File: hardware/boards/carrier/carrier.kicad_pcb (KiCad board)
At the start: 4 copper layers, 106 x 34.3 mm, 56 parts, among them J1 XT30PW(2+2), Q1 IPB020N10N5LF, Q2 2N7002, Q3 2N7002, SW1 SKSCLCE010, U1 STM32G031G6U6, U2 LM5163DDAR, U3 LMX5069MS, U4 INA237AIDGSR

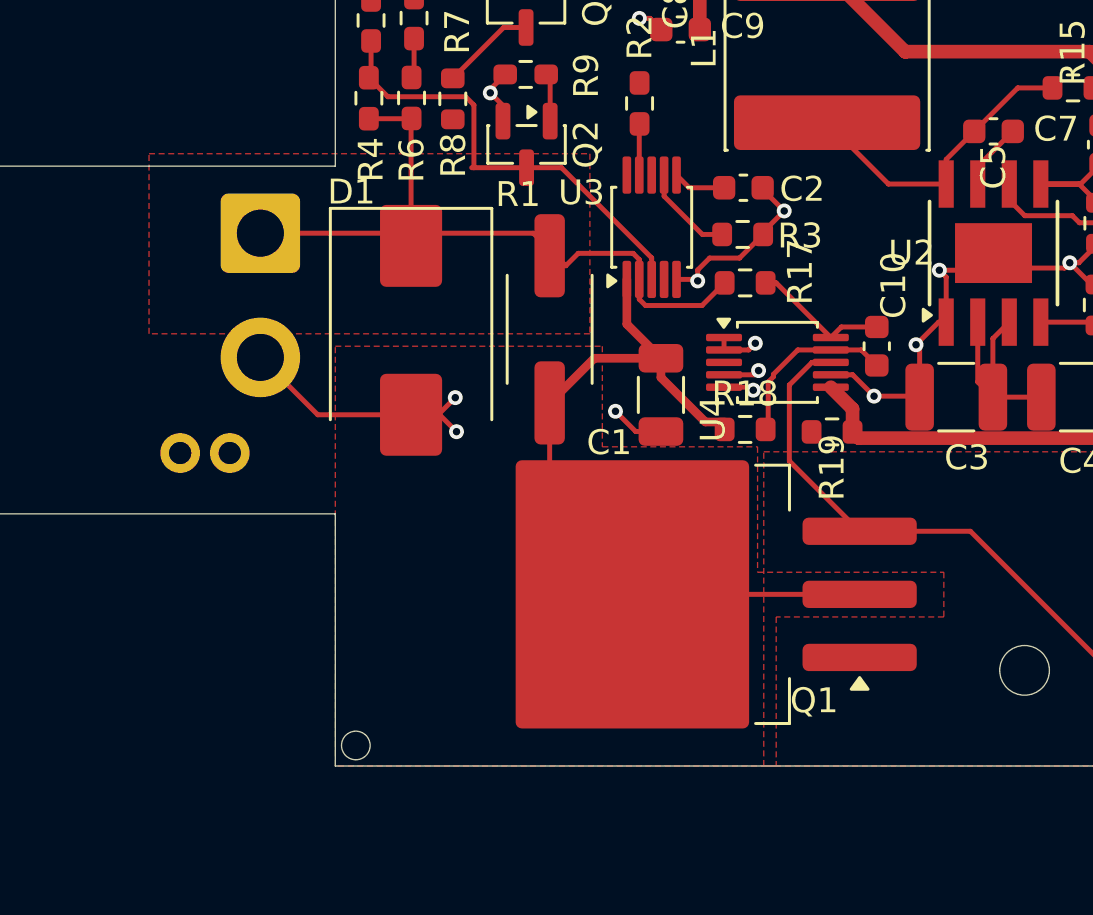
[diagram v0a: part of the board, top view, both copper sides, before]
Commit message: hardware: add HS_SENSE thermal plane and stitching vias
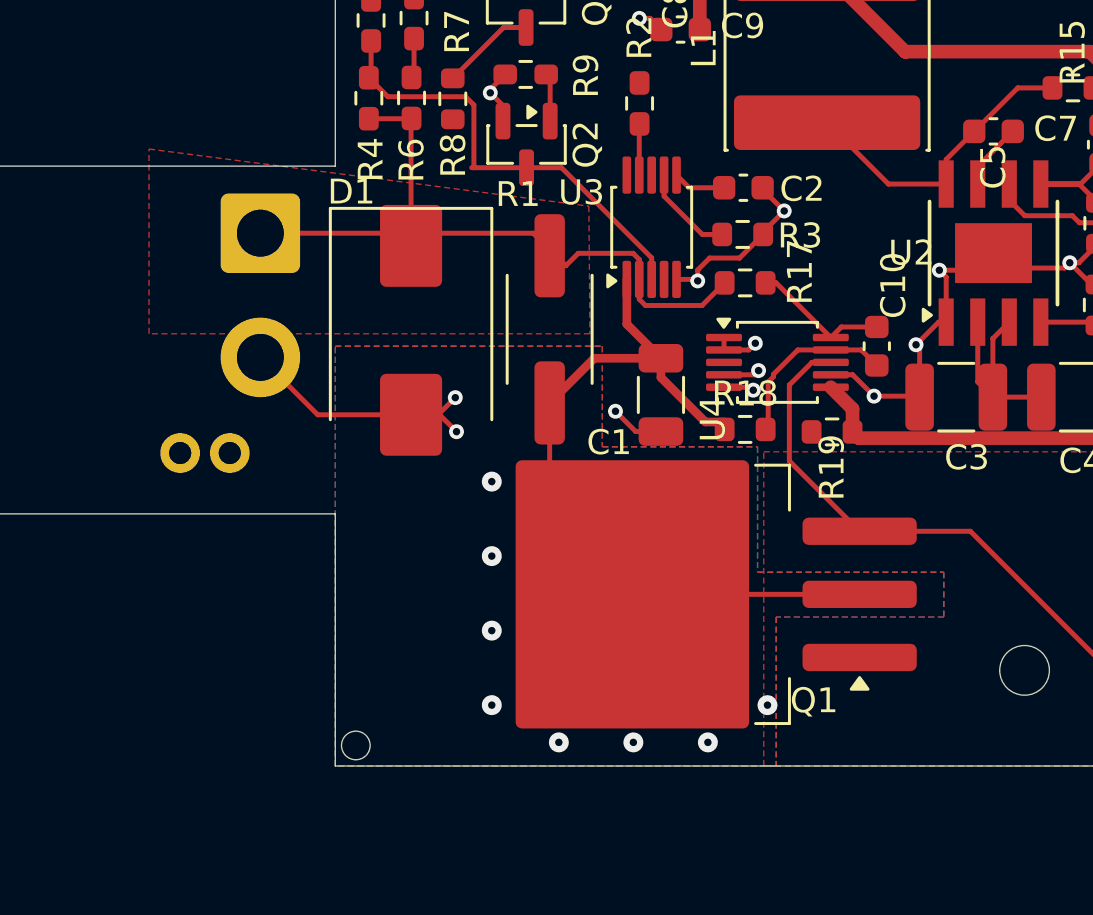
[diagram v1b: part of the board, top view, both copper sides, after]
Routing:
- net /Protected Power and Controls/HS_SENSE: vias 0 -> 8
- added copper zone on B.Cu, net /Protected Power and Controls/HS_SENSE
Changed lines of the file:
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@@
+		(net "/Protected Power and Controls/HS_SENSE")
+	)
+	(via
+		(at 121.8 128.2)
+		(size 0.8)
+		(drill 0.3)
+		(layers "F.Cu" "B.Cu")
+		(free yes)
+		(net "/Protected Power and Controls/HS_SENSE")
+	)
+	(via
+		(at 121.8 119.2)
+		(size 0.8)
+		(drill 0.3)
+		(layers "F.Cu" "B.Cu")
+		(free yes)
+		(net "/Protected Power and Controls/HS_SENSE")
+	)
+	(via
+		(at 121.8 125.2)
+		(size 0.8)
+		(drill 0.3)
+		(layers "F.Cu" "B.Cu")
+		(free yes)
+		(net "/Protected Power and Controls/HS_SENSE")
+	)
+	(via
+		(at 132.9 128.2)
+		(size 0.8)
+		(drill 0.3)
+		(layers "F.Cu" "B.Cu")
+		(free yes)
+		(net "/Protected Power and Controls/HS_SENSE")
+	)
+	(via
+		(at 130.5 129.7)
+		(size 0.8)
+		(drill 0.3)
+		(layers "F.Cu" "B.Cu")
+		(free yes)
+		(net "/Protected Power and Controls/HS_SENSE")
+	)
+	(via
+		(at 121.8 122.2)
+		(size 0.8)
+		(drill 0.3)
+		(layers "F.Cu" "B.Cu")
+		(free yes)
+		(net "/Protected Power and Controls/HS_SENSE")
+	)
+	(via
+		(at 124.5 129.7)
+		(size 0.8)
+		(drill 0.3)
+		(layers "F.Cu" "B.Cu")
+		(free yes)
+		(net "/Protected Power and Controls/HS_SENSE")
+	)
+	(via
+		(at 127.5 129.7)
+		(size 0.8)
+		(drill 0.3)
+		(layers "F.Cu" "B.Cu")
+		(free yes)
 		(net "/Protected Power and Controls/HS_SENSE")
 	)
@@
 		(layer "F.Cu")
 		(net "/STM32 Housekeeping and Status/NRST")
+	)
+	(zone
+		(net "/Protected Power and Controls/HS_SENSE")
+		(layer "F.Cu")
+		(name "HS_SENSE")
+		(hatch edge 0.5)
+		(priority 1)
+		(connect_pads
+			(clearance 0.5)
+		)
+		(min_thickness 0.25)
+		(fill yes
+			(thermal_gap 0.5)
+			(thermal_bridge_width 0.5)
+			(island_removal_mode 0)
+		)
+		(polygon
+			(pts
+				(xy 115.5 113.75) (xy 126.25 113.75) (xy 126.25 117.8) (xy 132.5 117.8) (xy 132.5 122.85) (xy 140 122.85)
+				(xy 140 124.65) (xy 133.25 124.65) (xy 133.25 130.65) (xy 115.5 130.65)
+			)
+		)
+	)
+	(zone
+		(net "VCC")
+		(layer "F.Cu")
+		(name "VCC")
+		(hatch edge 0.5)
+		(priority 2)
+		(connect_pads
+			(clearance 0.5)
+		)
+		(min_thickness 0.25)
+		(fill yes
+			(thermal_gap 0.5)
+			(thermal_bridge_width 0.5)
+			(island_removal_mode 0)
+		)
+		(polygon
+			(pts
+				(xy 108 105.810649) (xy 125.708468 108.11045) (xy 125.75 113.25) (xy 108 113.25)
+			)
+		)
+	)
+	(zone
+		(net "/Protected Power and Controls/PD_VIN_SW")
+		(layer "F.Cu")
+		(name "PD_VIN_SW")
+		(hatch edge 0.5)
+		(connect_pads
+			(clearance 0.5)
+		)
+		(min_thickness 0.25)
+		(fill yes
+			(thermal_gap 0.5)
+			(thermal_bridge_width 0.5)
+			(island_removal_mode 0)
+		)
+		(polygon
+			(pts
+				(xy 132.75 118) (xy 155.1 118) (xy 155.1 130.65) (xy 132.75 130.65)
+			)
+		)
+	)
+	(zone
+		(net "VCC")
+		(layer "F.Cu")
+		(hatch none 0.1)
+		(priority 30001)
+		(attr
+			(teardrop
+				(type padvia)
+			)
+		)
+		(connect_pads yes
+			(clearance 0)
+		)
+		(min_thickness 0.0254)
+		(fill yes
+			(island_removal_mode 1)
+		)
+		(polygon
+			(pts
+				(xy 115.0825 109.3) (xy 115.0825 109.1) (xy 114.0825 108.2) (xy 112.4815 109.2) (xy 114.0825 110.2)
+			)
+		)
 	)
 	(zone
@@
 	(zone
 		(net "/Protected Power and Controls/HS_SENSE")
-		(layer "F.Cu")
-		(name "HS_SENSE")
+		(layer "B.Cu")
+		(name "HS_SENSE_BOTTOM")
 		(hatch edge 0.5)
 		(priority 1)
@@
 		)
 		(min_thickness 0.25)
-		(fill
+		(fill yes
 			(thermal_gap 0.5)
 			(thermal_bridge_width 0.5)
@@
 		(polygon
 			(pts
-				(xy 115.5 113.75) (xy 126.25 113.75) (xy 126.25 117.8) (xy 132.5 117.8) (xy 132.5 122.85)
-				(xy 140 122.85) (xy 140 124.65) (xy 133.25 124.65) (xy 133.25 130.65) (xy 115.5 130.65)
+				(xy 115.5 113.75) (xy 126.25 113.75) (xy 126.25 117.8) (xy 132.5 117.8) (xy 132.5 122.85) (xy 140 122.85)
+				(xy 140 124.65) (xy 133.25 124.65) (xy 133.25 130.65) (xy 115.5 130.65)
 			)
 		)
-	)
-	(zone
-		(net "VCC")
-		(layer "F.Cu")
-		(name "VCC")
-		(hatch edge 0.5)
-		(priority 2)
-		(connect_pads
-			(clearance 0.5)
-		)
-		(min_thickness 0.25)
-		(fill
-			(thermal_gap 0.5)
-			(thermal_bridge_width 0.5)
-			(island_removal_mode 0)
-		)
-		(polygon
-			(pts
-				(xy 108 106) (xy 125.75 106) (xy 125.75 113.25) (xy 108 113.25)
-			)
-		)
-	)
-	(zone
-		(net "/Protected Power and Controls/PD_VIN_SW")
-		(layer "F.Cu")
-		(name "PD_VIN_SW")
-		(hatch edge 0.5)
-		(connect_pads
-			(clearance 0.5)
-		)
-		(min_thickness 0.25)
-		(fill
-			(thermal_gap 0.5)
-			(thermal_bridge_width 0.5)
-			(island_removal_mode 0)
-		)
-		(polygon
-			(pts
-				(xy 132.75 118) (xy 155.1 118) (xy 155.1 130.65) (xy 132.75 130.65)
-			)
-		)
-	)
-	(zone
-		(net "VCC")
-		(layer "F.Cu")
-		(hatch none 0.1)
-		(priority 30000)
-		(attr
-			(teardrop
-				(type padvia)
-			)
-		)
-		(connect_pads yes
-			(clearance 0)
-		)
-		(min_thickness 0.0254)
-		(fill yes
-			(island_removal_mode 1)
-		)
-		(polygon
-			(pts
-				(xy 115.0825 109.3) (xy 115.0825 109.1) (xy 114.0825 108.2) (xy 112.4815 109.2) (xy 114.0825 110.2)
-			)
-		)

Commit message: Checkpoint:
Routing is still ... in progress
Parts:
- moved J2 0.13 mm to (190.7, 98.2)
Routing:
- net /PD_ENABLE: track 65.3 -> 1.90 mm
- net +3V3: track 94.7 -> 157.3 mm
- net /STM32 Housekeeping and Status/SWCLK: track 0.00 -> 4.68 mm
- net /STM32 Housekeeping and Status/SWDIO: track 0.00 -> 4.56 mm
- net /BUCK_FB: track 7.71 -> 6.17 mm

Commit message: Replace carrier MCU with STM32C092GCU7
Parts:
- U1: value STM32G031G6U6 -> STM32C092GCU7
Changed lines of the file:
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@@
 			)
 		)
-		(property "Value" "STM32G031G6U6"
+		(property "Value" "STM32C092GCU7"
 			(at 0 3.33 0)
 			(layer "F.Fab")
@@
 			)
 		)
-		(property "Datasheet" "https://www.st.com/resource/en/datasheet/stm32g031g6.pdf"
+		(property "Datasheet" "https://www.st.com/resource/en/datasheet/stm32c092gc.pdf"
 			(at 0 0 0)
 			(layer "F.Fab")
@@
 			)
 		)
-		(property "Description" "STMicroelectronics Arm Cortex-M0+ MCU, 32KB flash, 8KB RAM, 64 MHz, 1.7-3.6V, 26 GPIO, UFQFPN28"
+		(property "Description" "STMicroelectronics Arm Cortex-M0+ MCU, 256KB flash, 30KB RAM, 48 MHz, 2.0-3.6V, FDCAN, 26 GPIO, UFQFPN28"
 			(at 0 0 0)
 			(layer "F.Fab")
@@
 			)
 		)
-		(property "MPN" "STM32G031G6U6"
+		(property "MPN" "STM32C092GCU7"
 			(at 0 0 0)
 			(unlocked yes)
@@
 			)
 		)
-		(property "LCSC" "C432210"
+		(property "LCSC" ""
 			(at 0 0 0)
 			(unlocked yes)

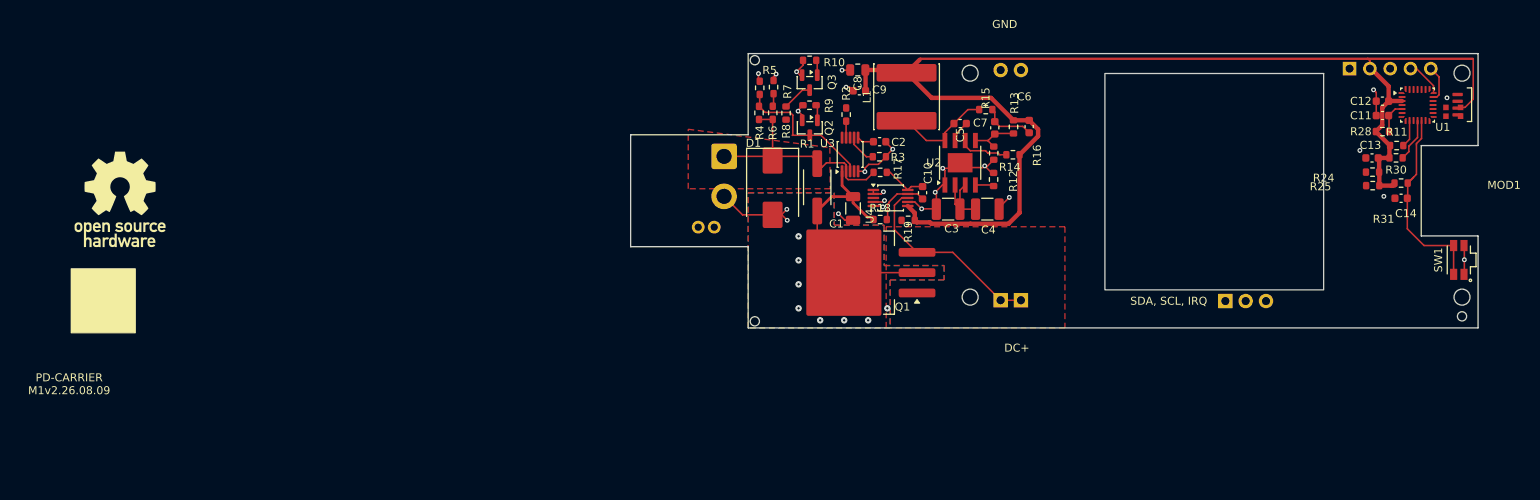
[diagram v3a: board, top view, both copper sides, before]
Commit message: Replace carrier backplane SMBus with CAN-FD
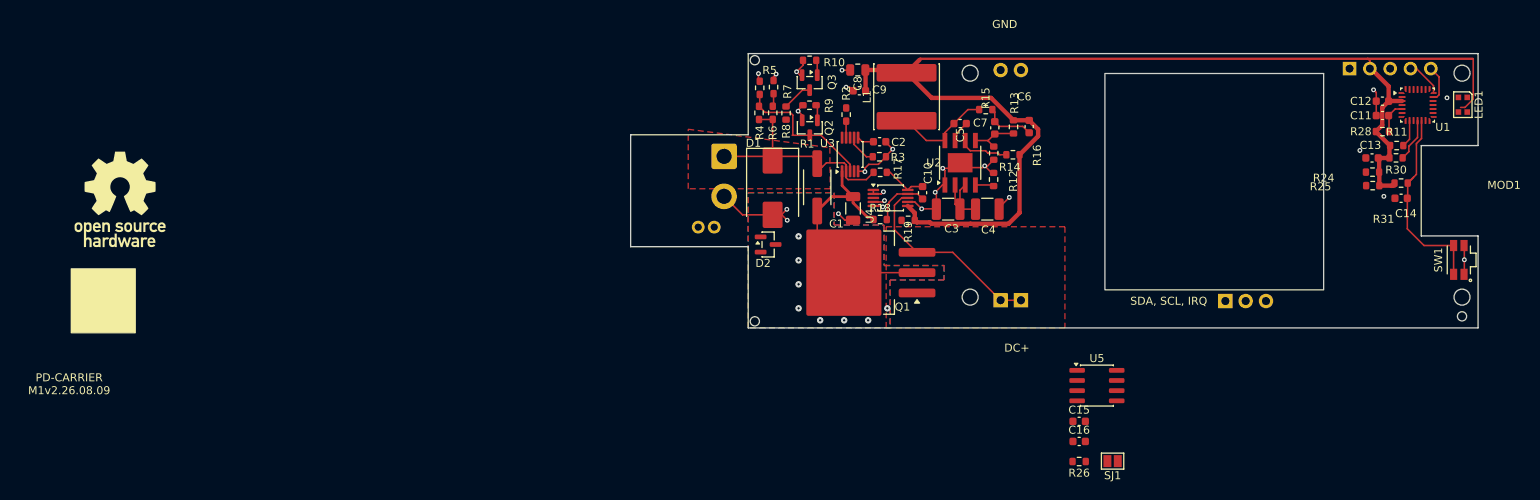
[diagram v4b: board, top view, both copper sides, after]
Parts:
- added C15: 100nF 100V, Capacitor_SMD:C_0603_1608Metric, F.Cu at (156.9, 142.3)
- added C16: 100nF 100V, Capacitor_SMD:C_0603_1608Metric, F.Cu at (156.9, 144.8)
- added D2: PESD2CANFD27V-TR, Package_TO_SOT_SMD:SOT-23, F.Cu at (118.0, 120.2)
- added R26: 120R 1%, Resistor_SMD:R_0603_1608Metric, F.Cu at (156.9, 147.4)
- added SJ1: CAN TERMINATE, Jumper:SolderJumper-2_P1.3mm_Open_Pad1.0x1.5mm, F.Cu at (161.1, 147.3)
- added U5: TCAN3413DR, Package_SO:SOIC-8_3.9x4.9mm_P1.27mm, F.Cu at (159.1, 137.9)
- LED1: value WS2812B-4020-V6 -> WS2812B-2020-V6; footprint mini-rack-power:LED_Worldsemi_WS2812B-4020_SideView -> LED_SMD:LED_WS2812B-2020_PLCC4_2.0x2.0mm
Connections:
- J1 pad 3: /BP_SMBUS_SDA -> /CANL_BUS
- J1 pad 4: /BP_SMBUS_SCL -> /CANH_BUS
- LED1 pad 1: /STM32 Housekeeping and Status/LED_DATA_RAW -> unconnected-(LED1-DOUT-Pad1)
- LED1 pad 2: +3V3 -> GND
- LED1 pad 3: unconnected-(LED1-DOUT-Pad3) -> /STM32 Housekeeping and Status/LED_DATA_RAW
- LED1 pad 4: GND -> +3V3
- U1 pad 10: /BUCK_PGOOD -> CAN_STB
- U1 pad 13: unconnected-(U1-PA7-Pad13) -> /BUCK_PGOOD
- U1 pad 18: /PD_I2C_SCL -> CAN_RX
- U1 pad 19: /PD_I2C_SDA -> CAN_TX
- U1 pad 26: /BP_SMBUS_SCL -> /PD_I2C_SCL
- U1 pad 27: /BP_SMBUS_SDA -> /PD_I2C_SDA

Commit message: Move carrier LED data to PA8
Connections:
- U1 pad 16: unconnected-(U1-PA8-Pad16) -> /STM32 Housekeeping and Status/LED_DATA_RAW
- U1 pad 6: /STM32 Housekeeping and Status/LED_DATA_RAW -> unconnected-(U1-PA0-Pad6)
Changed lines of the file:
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@@
 			(layers "F.Cu" "F.Mask" "F.Paste")
 			(roundrect_rratio 0.25)
-			(net "/STM32 Housekeeping and Status/LED_DATA_RAW")
+			(net "unconnected-(U1-PA0-Pad6)")
 			(pinfunction "PA0_6")
-			(pintype "bidirectional")
+			(pintype "bidirectional+no_connect")
 		)
 		(pad "7" smd custom
@@
 			(layers "F.Cu" "F.Mask" "F.Paste")
 			(roundrect_rratio 0.25)
-			(net "unconnected-(U1-PA8-Pad16)")
+			(net "/STM32 Housekeeping and Status/LED_DATA_RAW")
 			(pinfunction "PA8_16")
-			(pintype "bidirectional+no_connect")
+			(pintype "bidirectional")
 		)
 		(pad "17" smd roundrect
@@
 	)
 	(zone
-		(net "VCC")
-		(layer "F.Cu")
-		(hatch none 0.1)
-		(priority 30001)
-		(attr
-			(teardrop
-				(type padvia)
-			)
-		)
-		(connect_pads yes
-			(clearance 0)
-		)
-		(min_thickness 0.0254)
-		(fill yes
-			(island_removal_mode 1)
-		)
-		(polygon
-			(pts
-				(xy 115.0825 109.3) (xy 115.0825 109.1) (xy 114.0825 108.2) (xy 112.4815 109.2) (xy 114.0825 110.2)
-			)
-		)
-	)
-	(zone
 		(net "/Protected Power and Controls/HS_SENSE")
 		(layer "F.Cu")
@@
 			)
 		)
+	)
+	(zone
+		(net "VCC")
+		(layer "F.Cu")
+		(hatch none 0.1)
+		(priority 30001)
+		(attr
+			(teardrop
+				(type padvia)
+			)
+		)
+		(connect_pads yes
+			(clearance 0)
+		)
+		(min_thickness 0.0254)
+		(fill yes
+			(island_removal_mode 1)
+		)
+		(polygon
+			(pts
+				(xy 115.0825 109.3) (xy 115.0825 109.1) (xy 114.0825 108.2) (xy 112.4815 109.2) (xy 114.0825 110.2)
+			)
+		)

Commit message: Reposition carrier CAN hardware
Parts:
- added R26: 120R 1%, Resistor_SMD:R_0603_1608Metric, F.Cu at (184.0, 144.3)
- added TP5: GND, TestPoint:TestPoint_Pad_D1.0mm, F.Cu at (187.5, 144.5)
- SJ1: value CAN TERMINATE -> CAN TERMINATION
- moved SJ1 23.9 mm to (184.2, 141.2), turned to 0 degrees
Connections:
- net /Protected Power and Controls/CANH_PHY renamed Net-(L3-A_PHY)
- net /Protected Power and Controls/CANL_PHY renamed Net-(L3-B_PHY)
- D2 pad 1: /CANH_BUS -> /Protected Power and Controls/CANH_BUS
- D2 pad 2: /CANL_BUS -> /Protected Power and Controls/CANL_BUS
- U5 pad 3: +3V3 -> Net-(U5-VCC)
- U5 pad 5: +3V3 -> Net-(U5-VCC)
